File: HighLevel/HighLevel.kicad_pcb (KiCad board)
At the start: 2 copper layers, 134 parts, among them J1 USB_A, J10 UCC27210DDA, J2 Conn_01x06, J3 COMM, J8 UCC27210DDA, J9 UCC27210DDA, Q1 MOFSET_N, Q2 IPB039N10N3G, Q3 IPB039N10N3G, Q4 IPB039N10N3G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

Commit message: Added last two sheets and some footprints
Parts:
- added C55: 2.2u, Capacitor_SMD:C_0805_2012Metric, F.Cu at (200.6, 72.5)
- added C56: 2.2u, Capacitor_SMD:C_0805_2012Metric, F.Cu at (200.6, 75.5)
- added C57: 4.7u_100V, Capacitor_SMD:C_0805_2012Metric, F.Cu at (223.7, 73.3)
- added C58: 2.2u, Capacitor_SMD:C_0805_2012Metric, F.Cu at (200.6, 78.5)
- added C59: 100n, Capacitor_SMD:C_0805_2012Metric, F.Cu at (200.6, 81.5)
- added C60: 2.2u, Capacitor_SMD:C_0805_2012Metric, F.Cu at (200.6, 84.5)
- added C61: 10n, Capacitor_SMD:C_0805_2012Metric, F.Cu at (223.7, 76.3)
- added C62: 100n, Capacitor_SMD:C_0805_2012Metric, F.Cu at (223.7, 79.3)
- added C63: 2.2u, Capacitor_SMD:C_0805_2012Metric, F.Cu at (223.7, 82.3)
- added C64: 2.2u, Capacitor_SMD:C_0805_2012Metric, F.Cu at (223.7, 85.3)
- added C65: 22u_16V, Capacitor_SMD:CP_Elec_6.3x7.7, F.Cu at (231.2, 75.8)
- added L3: 100u, Inductor_SMD:L_0805_2012Metric, F.Cu at (232.6, 81.3)
- added R44: 1k, Resistor_SMD:R_0805_2012Metric, F.Cu at (205.0, 78.8)
- added R45: 402k, Resistor_SMD:R_0805_2012Metric, F.Cu at (228.1, 81.4)
- added R46: 1k, Resistor_SMD:R_0805_2012Metric, F.Cu at (205.0, 81.8)
- added R47: 10k, Resistor_SMD:R_0805_2012Metric, F.Cu at (228.1, 84.3)
- added R48: 2k, Resistor_SMD:R_0805_2012Metric, F.Cu at (228.1, 87.3)
- added U15: MPU-9150, Sensor_Motion:InvenSense_QFN-24_4x4mm_P0.5mm, F.Cu at (206.0, 74.2)
- added U16: LM5161PWP, Package_SO:HTSSOP-14-1EP_4.4x5mm_P0.65mm_EP3.4x5mm_Mask3x3.1mm, F.Cu at (215.6, 74.2)
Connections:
- net /driver/HI1 renamed /MCU/H1
- net /driver/HI2 renamed /MCU/H2
- net /driver/HI3 renamed /MCU/H3
- net /driver/LI1 renamed /MCU/L1
- net /driver/LI2 renamed /MCU/L2
- net /driver/LI3 renamed /MCU/L3
- net /driver/SENS_1 renamed /MCU/Voltage_1
- net /driver/SENS_2 renamed /MCU/Voltage_2
- net /driver/SENS_3 renamed /MCU/Voltage_3
- net /driver/SENS_FILTER renamed /MCU/PC9
- net /driver/SENS_SUPPLY renamed /MCU/AN_IN
- net /mcu/ADC_15 renamed /MCU/ADC_15
- net /mcu/ADC_TEMP renamed /MCU/ADC_TEMP
- net /mcu/ADC_TEMP2 renamed /MCU/ADC_TEMP2
- net /mcu/ADC_TEMP3 renamed /MCU/ADC_TEMP3
- net /mcu/CURRENT_1 renamed /MCU/CURRENT_1
- net /mcu/CURRENT_2 renamed /MCU/CURRENT_2
- net /mcu/CURRENT_3 renamed /MCU/CURRENT_3
- net /mcu/CURR_FILTER renamed /MCU/CURR_FILTER
- net /mcu/HALL_1 renamed /MCU/HALL_1
- net /mcu/HALL_2 renamed /MCU/HALL_2
- net /mcu/HALL_3 renamed /MCU/HALL_3
- net /mcu/LED_GREEN renamed /MCU/LED_GREEN
- net /mcu/LED_RED renamed /MCU/LED_RED
- net /mcu/MISO_ADC_EXT2 renamed /MCU/MISO_ADC_EXT2
- net /mcu/NRST renamed /MCU/NRST
- net /mcu/PC13 renamed /MCU/PC13
- net /mcu/RX_SDA_NSS renamed /IMU/SDA
- net /mcu/SCK_ADC_EXT renamed /MCU/SCK_ADC_EXT
- net /mcu/SERVO renamed /MCU/SERVO
- net /mcu/SPI3_CE renamed /MCU/SPI3_CE
- net /mcu/SPI3_CSN renamed /MCU/SPI3_CSN
- net /mcu/SPI3_MISO renamed /MCU/SPI3_MISO
- net /mcu/SPI3_MOSI renamed /MCU/SPI3_MOSI
- net /mcu/SPI3_SCK renamed /MCU/SPI3_SCK
- net /mcu/SWCLK renamed /MCU/SWCLK
- net /mcu/SWDIO renamed /MCU/SWDIO
- net /mcu/TEMP_MOTOR renamed /MCU/TEMP_MOTOR
- net /mcu/TX_SCL_MOSI renamed /IMU/SCL
- net /mcu/USB_DM renamed /MCU/USB_DM
- net /mcu/USB_DP renamed /MCU/USB_DP

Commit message: Arranged components on PCB
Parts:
- moved R45 166.6 mm to (63.3, 57.4), turned to 90 degrees
- moved C52 164.5 mm to (30.5, 178.1), turned to 90 degrees
- moved C57 162.6 mm to (62.5, 52.2), turned to 180 degrees
- moved C61 161.9 mm to (62.5, 61.2), turned to 180 degrees
- moved C65 158.1 mm to (76.4, 43.5)
- moved C42 157.7 mm to (35.8, 181.1)
- moved L3 156.6 mm to (78.8, 52.4)
- moved C45 156.4 mm to (33.3, 185.8), turned to -90 degrees
- moved C64 154.0 mm to (73.9, 49.8), turned to 180 degrees
- moved R38 148.1 mm to (25.4, 176.5), turned to 90 degrees
- moved R41 145.8 mm to (25.4, 181.6)
- moved C36 145.2 mm to (27.9, 162.6)
- moved R26 145.1 mm to (15.2, 157.1), turned to 90 degrees
- moved R47 143.5 mm to (88.2, 52.4)
- moved U16 143.5 mm to (73.1, 56.7)
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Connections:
- C56 pad 1: unconnected-(C56-Pad1) -> VCC

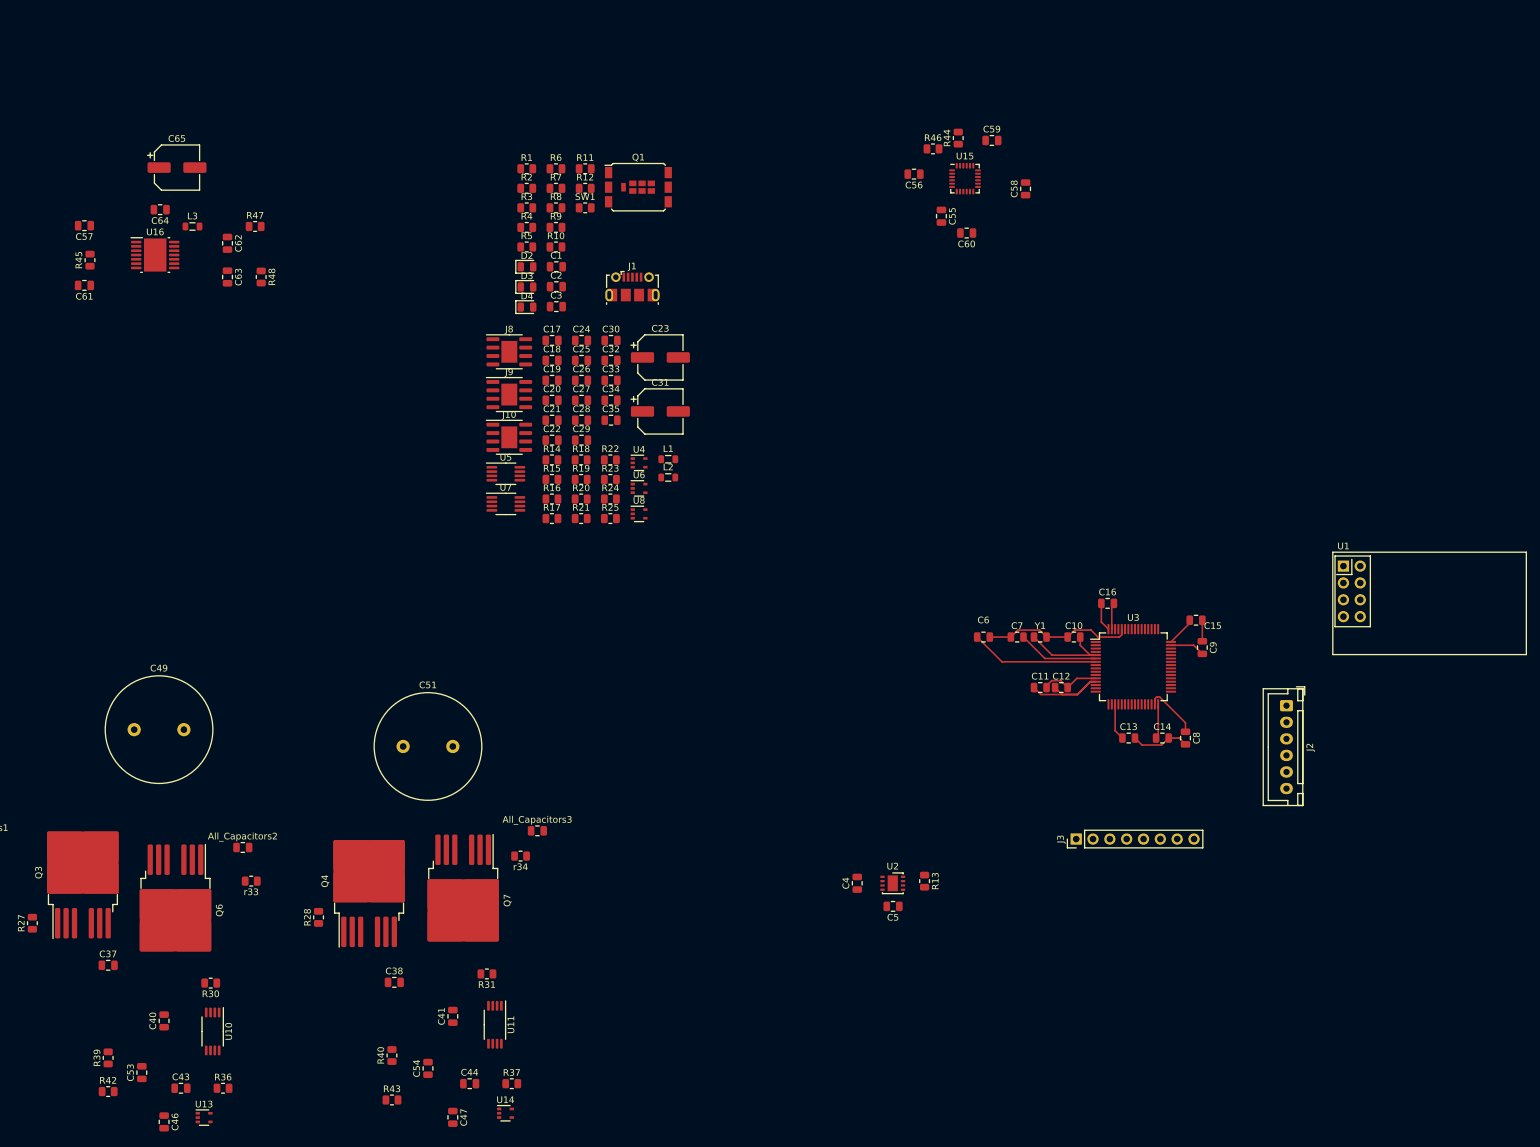
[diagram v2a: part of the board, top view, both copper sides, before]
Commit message: Updated Driver on PCB
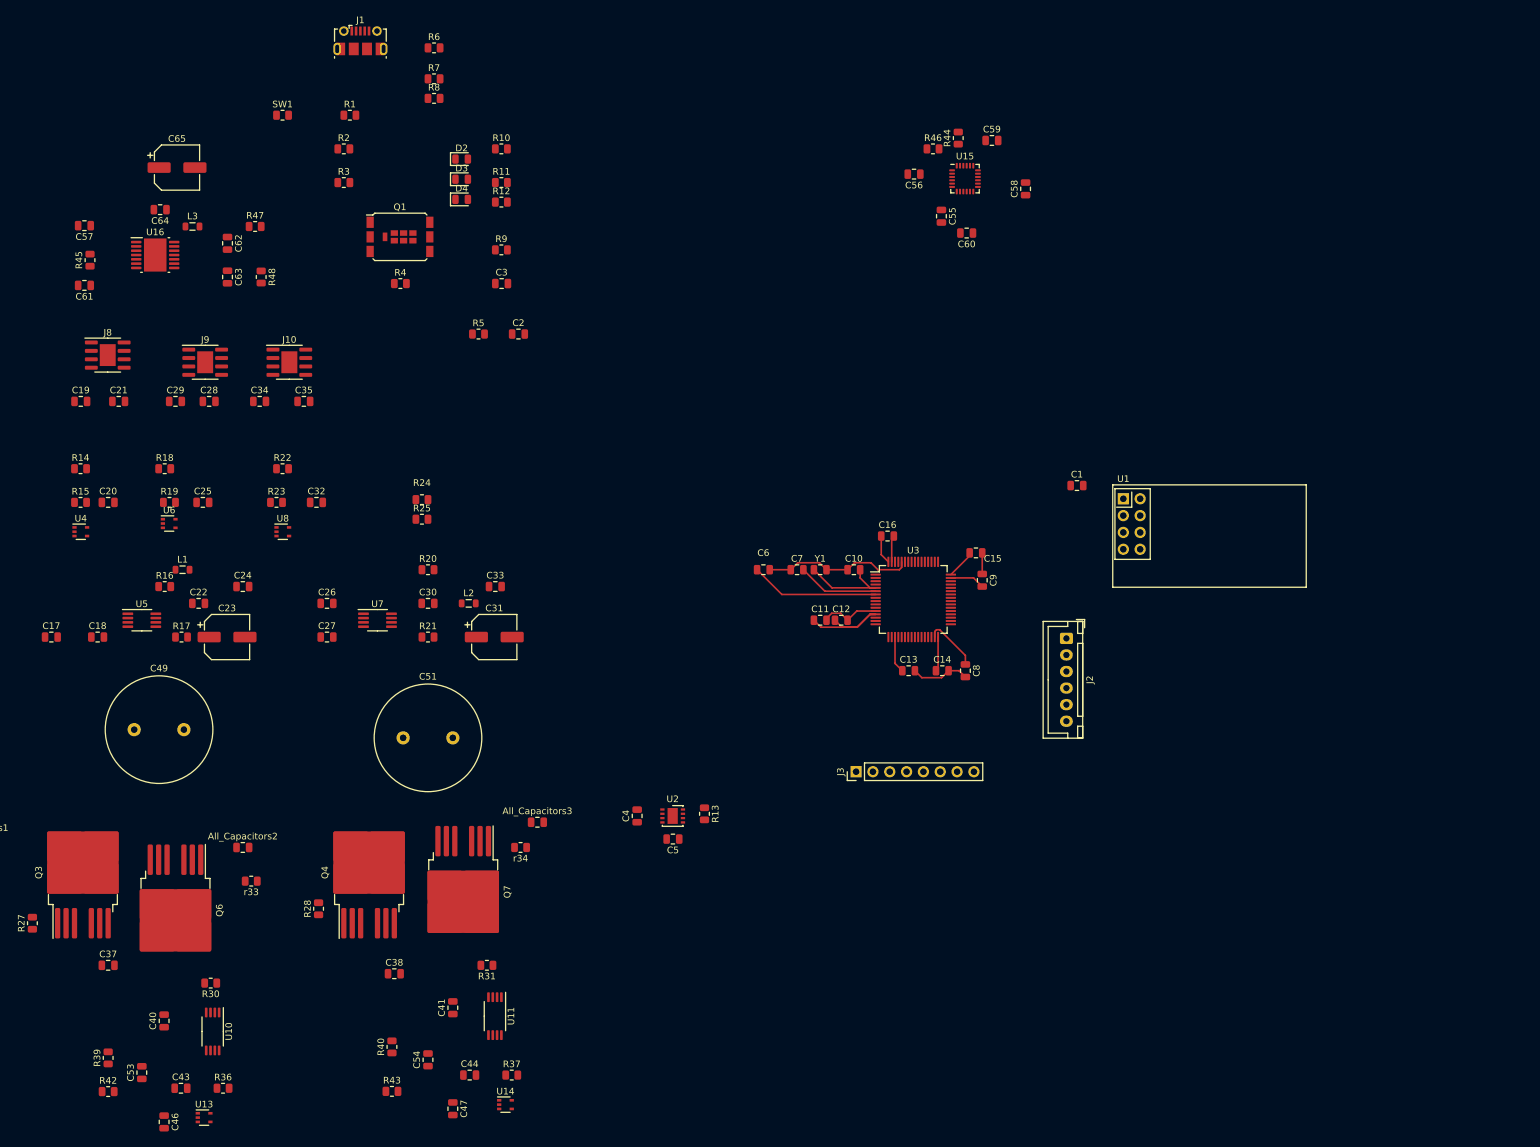
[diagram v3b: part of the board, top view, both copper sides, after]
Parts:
- moved C17 87.8 mm to (57.5, 114.3)
- moved C1 85.2 mm to (212.2, 91.4)
- moved U4 84.9 mm to (61.9, 98.4)
- moved C18 80.3 mm to (64.5, 114.3)
- moved C23 77.8 mm to (84.0, 114.3)
- moved L1 75.2 mm to (77.3, 104.1)
- moved R15 71.2 mm to (61.9, 94.0)
- moved C19 71.2 mm to (61.9, 78.7)
- moved R14 71.1 mm to (61.9, 88.9)
- moved U6 71.1 mm to (75.2, 97.2)
- moved C20 68.7 mm to (66.0, 94.0)
- moved C21 65.5 mm to (67.6, 78.7)
- moved C24 63.2 mm to (86.4, 106.7)
- moved R18 62.9 mm to (74.6, 88.9)
- moved R19 62.2 mm to (75.3, 94.0)
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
